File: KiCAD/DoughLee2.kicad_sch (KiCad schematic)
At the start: 34 parts, among them J1 Conn_01x06, U1 SHTC3, U4 SN74LVC1G123DCUR, U5 74LVC1G08

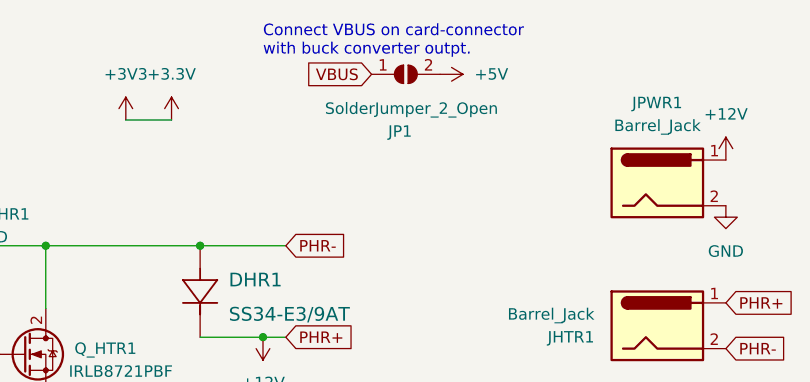
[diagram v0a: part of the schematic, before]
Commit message: Updated KiCAD design
- Fix library locations
- Update some footprints and symbols
- Added missing +3.3V to SHTC3
- Removed jumper from edge-connector power and replaced with wire
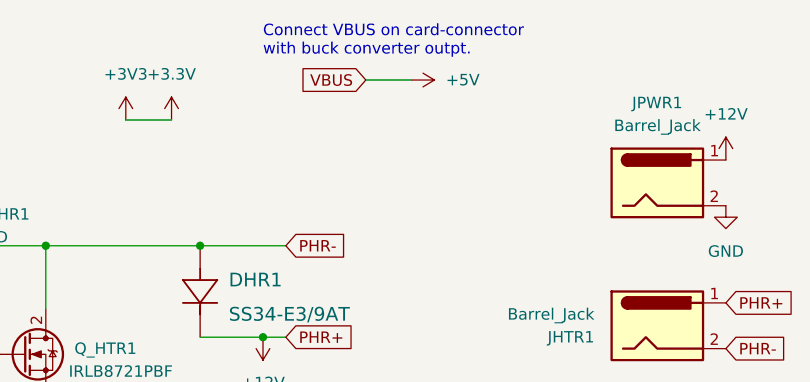
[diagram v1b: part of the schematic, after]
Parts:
- removed JP1: SolderJumper_2_Open, Jumper:SolderJumper-2_P1.3mm_Open_Pad1.0x1.5mm, symbol Jumper:SolderJumper_2_Open
- DHR1: footprint CR_3/9AT_VIS -> Diode_SMD:D_SMB
- U4: footprint Library:SOP50P310X90-8N -> chl33_library:SOP50P310X90-8N
- U5: footprint Library:SOT-23-5 -> chl33_library:SOT-23-5
